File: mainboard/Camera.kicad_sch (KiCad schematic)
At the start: 11 parts, among them IC1201 TXB0102DCU, IC1202 PCA9306JK, X1201 Camera, Y1201 25 MHz

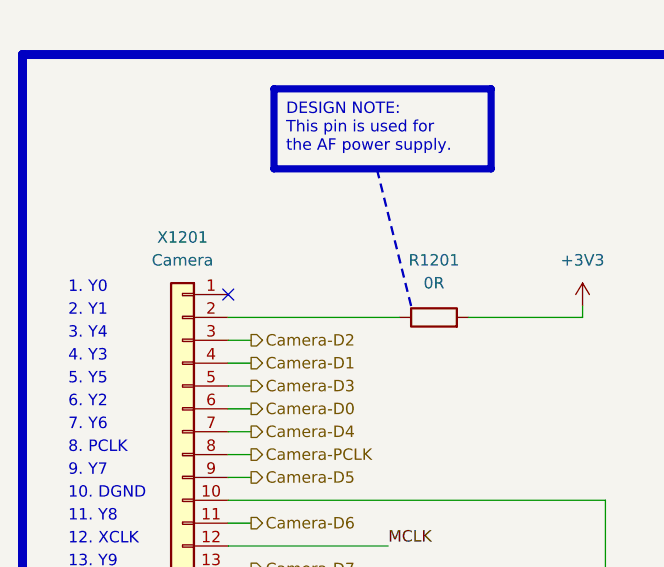
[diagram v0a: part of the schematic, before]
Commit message: Added: Add optional GND connection for camera AF on pin 24
- Some camera module require a GND connection on this pin
- CHANGELOG fixes

Signed-off-by: Daniel Kampert <DanielKampert@kampis-elektroecke.de>
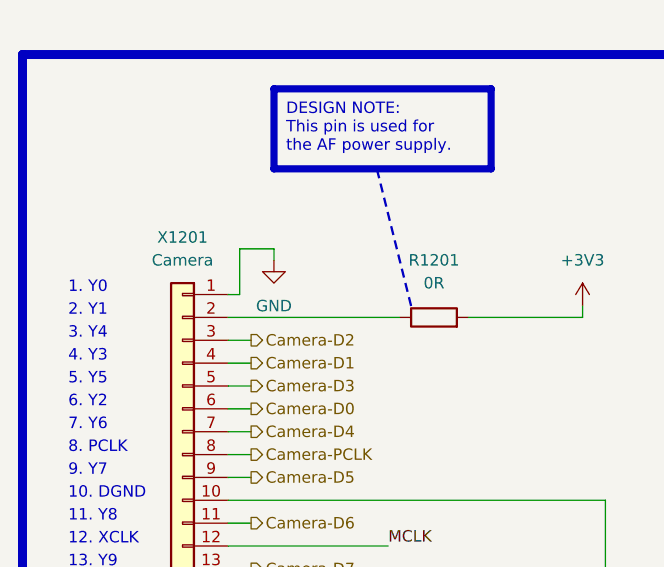
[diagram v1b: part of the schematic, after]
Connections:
- net GND: now also X1201.1 (Pin_1)
- no-connect marks 2 -> 1
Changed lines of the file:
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@@
-	)
-	(no_connect
-		(at 36.83 60.96)
 	)
 	(no_connect
@@
 	(wire
 		(pts
+			(xy 38.1 55.88) (xy 41.91 55.88)
+		)
+		(stroke
+			(width 0)
+			(type default)
+		)
+	)
+	(wire
+		(pts
 			(xy 36.83 76.2) (xy 39.37 76.2)
 		)
@@
 	(wire
 		(pts
+			(xy 41.91 55.88) (xy 41.91 57.15)
+		)
+		(stroke
+			(width 0)
+			(type default)
+		)
+	)
+	(wire
+		(pts
 			(xy 209.55 102.87) (xy 215.9 102.87)
 		)
@@
 	(wire
 		(pts
+			(xy 38.1 60.96) (xy 38.1 55.88)
+		)
+		(stroke
+			(width 0)
+			(type default)
+		)
+	)
+	(wire
+		(pts
 			(xy 219.71 107.95) (xy 219.71 109.22)
 		)
@@
 			(width 0.1524)
 			(type solid)
+		)
+	)
+	(wire
+		(pts
+			(xy 36.83 60.96) (xy 38.1 60.96)
+		)
+		(stroke
+			(width 0)
+			(type default)
 		)
 	)
@@
 					(unit 1)
 				)
+			)
+		)
+	)
+	(symbol
+		(lib_id "power:GND")
+		(at 41.91 57.15 0)
+		(unit 1)
+		(exclude_from_sim no)
+		(in_bom yes)
+		(on_board yes)
+		(dnp no)
+		(fields_autoplaced yes)
+		(property "Reference" "#PWR01213"
+			(at 41.91 63.5 0)
+			(effects
+				(font
+					(size 1.27 1.27)
+				)
+				(hide yes)
+			)
+		)
+		(property "Value" "GND"
+			(at 41.91 62.23 0)
+			(effects
+				(font
+					(size 1.27 1.27)
+				)
+			)
+		)
+		(property "Footprint" ""
+			(at 41.91 57.15 0)
+			(effects
+				(font
+					(size 1.27 1.27)
+				)
+				(hide yes)
+			)
+		)
+		(property "Datasheet" ""
+			(at 41.91 57.15 0)
+			(effects
+				(font
+					(size 1.27 1.27)
+				)
+				(hide yes)
+			)
+		)
+		(property "Description" "Power symbol creates a global label with name \"GND\" , ground"
+			(at 41.91 57.15 0)
+			(effects
+				(font
+					(size 1.27 1.27)
+				)
+				(hide yes)
+			)
+		)
+		(pin "1"
+		)
+		(instances
+			(project "Mainboard"
+				(path "/d5742f03-3b1a-42e5-a384-018bd4b919aa/c5103ceb-5325-4a84-a025-9638a412984e/b241b90d-ce8f-4ac5-a13c-a4133ff3ac6b"
+					(reference "#PWR01213")
+					(unit 1)
+				)
